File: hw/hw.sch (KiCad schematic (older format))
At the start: 36 parts, among them U1 74LS32, U10 74LS74, U2 Z80CPU, U3 74LS138, U4 74LS08, U5 CY7C199, U6 74LS299, U7 74HCT574, U8 74LS161, U9 74LS245, X1 CXO_DIP8

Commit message: move over to dedicated AVR
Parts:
- removed A1: Arduino_Nano_v3.x, Module:Arduino_Nano, symbol MCU_Module:Arduino_Nano_v3.x
- removed D1: 1N4148, Diode_THT:D_DO-35_SOD27_P7.62mm_Horizontal, symbol Diode:1N4148
- added C? (x2): 10n, symbol Device:C_Small
- added J?: Conn_02x03_Odd_Even, symbol Connector_Generic:Conn_02x03_Odd_Even
- added R?: 4K7, symbol Device:R
- added U?: ATmega328P-PU, Package_DIP:DIP-28_W7.62mm, symbol MCU_Microchip_ATmega:ATmega328P-PU
- added U? (x2): 74LS74, symbol 74xx:74LS74
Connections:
- net labels added: CLK_AVR, ISP_MISO, ISP_MOSI, ISP_RESET, ISP_SCLK, VIS, VIS_RAW
- wire segments 343 -> 383
- no-connect marks 30 -> 19
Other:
- note added: "ARDUINO at 0x80\nPORTA at 0x81"
- note added: "Close to pins 20 and 7"
- note added: "FIXME: delete this\n"

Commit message: got video display working well
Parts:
- removed U? (x2): 74LS74, symbol 74xx:74LS74
- added U?: 74LS74, symbol 74xx:74LS74
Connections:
- net VIS_RAW is gone; now on net VIS: U?.5 (PD3)
- net +5V: now also U?.1 (~R), U?.4 (~S)
- net CHAR_TC: now also U?.3 (C)
- net HSYNC: now also U?.5 (Q)
- net HSYNC_RAW: now also U?.2 (D)
- no-connect marks 19 -> 18
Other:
- note removed: "FIXME: delete this\n"
- note removed: "FIXME: sync vsync to hsync?"
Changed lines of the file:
@@
 Text GLabel 7000 5700 0    50   Input ~ 0
 ~DPY_PL
-Text Notes 12100 1600 0    50   ~ 0
-FIXME: sync vsync to hsync?
 $Comp
 L Connector:DB15_Female_HighDensity_MountingHoles J?
@@
 Wire Wire Line
 	-700 10100 -800 10100
-Text Notes 13800 1700 0    50   ~ 0
-FIXME: delete this\n
 Text GLabel -700 8100 2    50   Output ~ 0
 VSYNC
@@
 	-700 8100 -800 8100
 Text GLabel -700 9900 2    50   Output ~ 0
-VIS_RAW
+VIS
 Wire Wire Line
 	-700 9900 -800 9900
@@
 $Comp
 L 74xx:74LS74 U?
-U 2 1 5E1749F3
-P 17400 3200
-F 0 "U?" H 17250 3450 50  0000 C CNN
-F 1 "74LS74" H 17550 3450 50  0000 C CNN
-F 2 "" H 17400 3200 50  0001 C CNN
-F 3 "74xx/74hc_hct74.pdf" H 17400 3200 50  0001 C CNN
-	2    17400 3200
-	1    0    0    -1
-$EndComp
-$Comp
-L 74xx:74LS74 U?
-U 1 1 5E174A95
-P 17400 4300
-F 0 "U?" H 17250 4550 50  0000 C CNN
-F 1 "74LS74" H 17550 4550 50  0000 C CNN
-F 2 "" H 17400 4300 50  0001 C CNN
-F 3 "74xx/74hc_hct74.pdf" H 17400 4300 50  0001 C CNN
-	1    17400 4300
-	1    0    0    -1
-$EndComp
-Text GLabel 16900 4200 0    50   Input ~ 0
+U 1 1 5E5262C9
+P 15000 1300
+F 0 "U?" H 14850 1550 50  0000 C CNN
+F 1 "74LS74" H 15150 1550 50  0000 C CNN
+F 2 "" H 15000 1300 50  0001 C CNN
+F 3 "74xx/74hc_hct74.pdf" H 15000 1300 50  0001 C CNN
+	1    15000 1300
+	1    0    0    -1
+$EndComp
+Wire Wire Line
+	15000 900  15000 1000
+Wire Wire Line
+	14700 1200 14600 1200
+Wire Wire Line
+	14600 1700 15000 1700
+Wire Wire Line
+	15300 1200 15500 1200
+Text GLabel 15500 1200 2    50   Output ~ 0
+HSYNC
+Wire Wire Line
+	14600 1300 14700 1300
+Wire Wire Line
+	15000 1700 15000 1600
+$Comp
+L power:+5V #PWR?
+U 1 1 5E5262D6
+P 15000 900
+F 0 "#PWR?" H 15000 750 50  0001 C CNN
+F 1 "+5V" H 15015 1073 50  0000 C CNN
+F 2 "" H 15000 900 50  0001 C CNN
+F 3 "" H 15000 900 50  0001 C CNN
+	1    15000 900
+	1    0    0    -1
+$EndComp
+Text GLabel 14600 1200 0    50   Input ~ 0
 HSYNC_RAW
-Text GLabel 16900 3100 0    50   Input ~ 0
-VIS_RAW
-Wire Wire Line
-	16900 4200 17100 4200
-Wire Wire Line
-	16900 3100 17100 3100
-$Comp
-L power:+5V #PWR?
-U 1 1 5E28AFBB
-P 17400 2800
-F 0 "#PWR?" H 17400 2650 50  0001 C CNN
-F 1 "+5V" H 17415 2973 50  0000 C CNN
-F 2 "" H 17400 2800 50  0001 C CNN
-F 3 "" H 17400 2800 50  0001 C CNN
-	1    17400 2800
-	1    0    0    -1
-$EndComp
-Wire Wire Line
-	17400 2800 17400 2900
-$Comp
-L power:+5V #PWR?
-U 1 1 5E2B9A1E
-P 17400 3900
-F 0 "#PWR?" H 17400 3750 50  0001 C CNN
-F 1 "+5V" H 17415 4073 50  0000 C CNN
-F 2 "" H 17400 3900 50  0001 C CNN
-F 3 "" H 17400 3900 50  0001 C CNN
-	1    17400 3900
-	1    0    0    -1
-$EndComp
-Wire Wire Line
-	17400 3900 17400 4000
-$Comp
-L power:+5V #PWR?
-U 1 1 5E345A93
-P 17800 3500
-F 0 "#PWR?" H 17800 3350 50  0001 C CNN
-F 1 "+5V" H 17815 3673 50  0000 C CNN
-F 2 "" H 17800 3500 50  0001 C CNN
-F 3 "" H 17800 3500 50  0001 C CNN
-	1    17800 3500
-	1    0    0    -1
-$EndComp
-Wire Wire Line
-	17800 3500 17800 3550
-Wire Wire Line
-	17800 3550 17400 3550
-Wire Wire Line
-	17400 3550 17400 3500
-$Comp
-L power:+5V #PWR?
-U 1 1 5E374AC3
-P 17800 4600
-F 0 "#PWR?" H 17800 4450 50  0001 C CNN
-F 1 "+5V" H 17815 4773 50  0000 C CNN
-F 2 "" H 17800 4600 50  0001 C CNN
-F 3 "" H 17800 4600 50  0001 C CNN
-	1    17800 4600
-	1    0    0    -1
-$EndComp
-Wire Wire Line
-	17800 4600 17800 4650
-Wire Wire Line
-	17800 4650 17400 4650
-Wire Wire Line
-	17400 4650 17400 4600
-NoConn ~ 17700 4400
-NoConn ~ 17700 3300
-Text GLabel 17800 4200 2    50   Output ~ 0
-HSYNC
-Wire Wire Line
-	17800 4200 17700 4200
-Text GLabel 17800 3100 2    50   Output ~ 0
-VIS
-Wire Wire Line
-	17800 3100 17700 3100
-Text GLabel 16900 3300 0    50   Input ~ 0
+Text GLabel 14600 1300 0    50   Input ~ 0
 CHAR_TC
-Wire Wire Line
-	17100 3200 17000 3200
-Wire Wire Line
-	17000 3200 17000 3300
-Wire Wire Line
-	17000 3300 16900 3300
-Text GLabel 16900 4400 0    50   Input ~ 0
-CHAR_TC
-Wire Wire Line
-	17100 4300 17000 4300
-Wire Wire Line
-	17000 4300 17000 4400
-Wire Wire Line
-	17000 4400 16900 4400
+$Comp
+L power:+5V #PWR?
+U 1 1 5E5B3D83
+P 14600 1700
+F 0 "#PWR?" H 14600 1550 50  0001 C CNN
+F 1 "+5V" H 14615 1873 50  0000 C CNN
+F 2 "" H 14600 1700 50  0001 C CNN
+F 3 "" H 14600 1700 50  0001 C CNN
+	1    14600 1700
+	1    0    0    -1
+$EndComp
+NoConn ~ 15300 1400
 $EndSCHEMATC

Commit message: got stable screen display and demo program
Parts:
- added RN?: R_Network08_US, Resistor_THT:R_Array_SIP9, symbol Device:R_Network08_US
- added U?: 74LS32, symbol 74xx:74LS32
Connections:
- net D0: now also RN?.9 (R8)
- net D1: now also RN?.8 (R7)
- net D2: now also RN?.7 (R6)
- net D3: now also RN?.6 (R5)
- net D4: now also RN?.5 (R4)
- net D5: now also RN?.4 (R3)
- net D6: now also RN?.3 (R2)
- net D7: now also RN?.2 (R1)
- net GND: now also RN?.1 (common)
- net ~MEM_REQ: now also U?.4
- net ~REFRESH: now also U?.5; no longer U?.11 (Cp)
- new net ~RFSH_VALID: U?.11 (Cp), U?.6
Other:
- note added: "Open Question: sync VIS to CHAR_TC?"
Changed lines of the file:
@@
 	5600 5500 5500 5500
 Text GLabel 5500 5650 0    50   Input ~ 0
-~REFRESH
+~RFSH_VALID
 Wire Wire Line
 	5500 5650 5550 5650
@@
 $EndComp
 NoConn ~ 15300 1400
+Wire Wire Line
+	15100 6600 14900 6600
+Wire Wire Line
+	14900 6700 15100 6700
+Wire Wire Line
+	14900 6800 15100 6800
+Wire Wire Line
+	15100 6900 14900 6900
+Wire Wire Line
+	14900 7000 15100 7000
+Wire Wire Line
+	15100 7100 14900 7100
+Wire Wire Line
+	14900 7200 15100 7200
+Wire Wire Line
+	15100 7300 14900 7300
+$Comp
+L Device:R_Network08_US RN?
+U 1 1 5E64502A
+P 15300 6900
+F 0 "RN?" V 15817 6900 50  0000 C CNN
+F 1 "R_Network08_US" V 15726 6900 50  0000 C CNN
+F 2 "Resistor_THT:R_Array_SIP9" V 15775 6900 50  0001 C CNN
+F 3 "http://www.vishay.com/docs/31509/csc.pdf" H 15300 6900 50  0001 C CNN
+	1    15300 6900
+	0    1    -1   0
+$EndComp
+$Comp
+L power:GND #PWR?
+U 1 1 5E645031
+P 15600 7400
+F 0 "#PWR?" H 15600 7150 50  0001 C CNN
+F 1 "GND" H 15605 7227 50  0000 C CNN
+F 2 "" H 15600 7400 50  0001 C CNN
+F 3 "" H 15600 7400 50  0001 C CNN
+	1    15600 7400
+	1    0    0    -1
+$EndComp
+Wire Wire Line
+	15500 7300 15600 7300
+Wire Wire Line
+	15600 7300 15600 7400
+Text GLabel 14900 6600 0    50   BiDi ~ 0
+D0
+Text GLabel 14900 6700 0    50   BiDi ~ 0
+D1
+Text GLabel 14900 6800 0    50   BiDi ~ 0
+D2
+Text GLabel 14900 6900 0    50   BiDi ~ 0
+D3
+Text GLabel 14900 7000 0    50   BiDi ~ 0
+D4
+Text GLabel 14900 7100 0    50   BiDi ~ 0
+D5
+Text GLabel 14900 7200 0    50   BiDi ~ 0
+D6
+Text GLabel 14900 7300 0    50   BiDi ~ 0
+D7
+Text GLabel 1400 8800 0    50   Input ~ 0
+~MEM_REQ
+Text GLabel 1400 9000 0    50   Input ~ 0
+~REFRESH
+$Comp
+L 74xx:74LS32 U?
+U 2 1 5E76DC2D
+P 1900 8900
+F 0 "U?" H 1900 9225 50  0000 C CNN
+F 1 "74LS32" H 1900 9134 50  0000 C CNN
+F 2 "" H 1900 8900 50  0001 C CNN
+F 3 "http://www.ti.com/lit/gpn/sn74LS32" H 1900 8900 50  0001 C CNN
+	2    1900 8900
+	1    0    0    -1
+$EndComp
+Wire Wire Line
+	1400 9000 1600 9000
+Wire Wire Line
+	1600 8800 1400 8800
+Text GLabel 2400 8900 2    50   Output ~ 0
+~RFSH_VALID
+Wire Wire Line
+	2400 8900 2200 8900
+Text Notes 15400 1750 0    50   ~ 0
+Open Question: sync VIS to CHAR_TC?
 $EndSCHEMATC

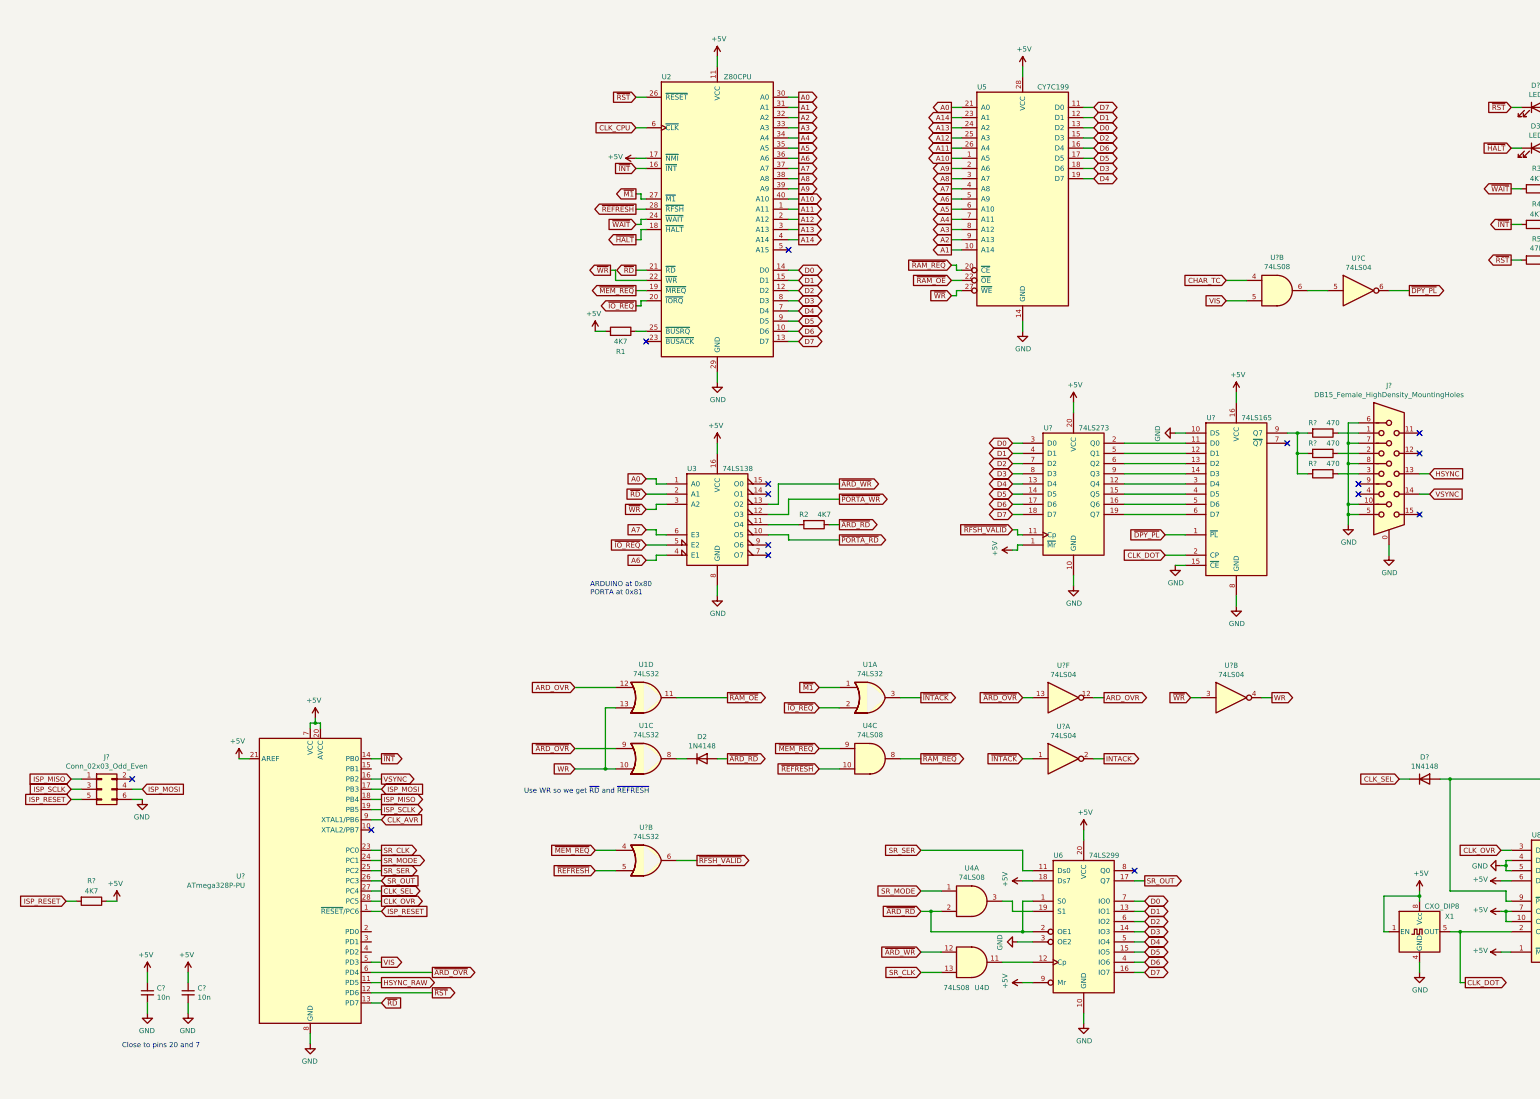
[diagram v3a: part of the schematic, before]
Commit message: fix schematic to match reality
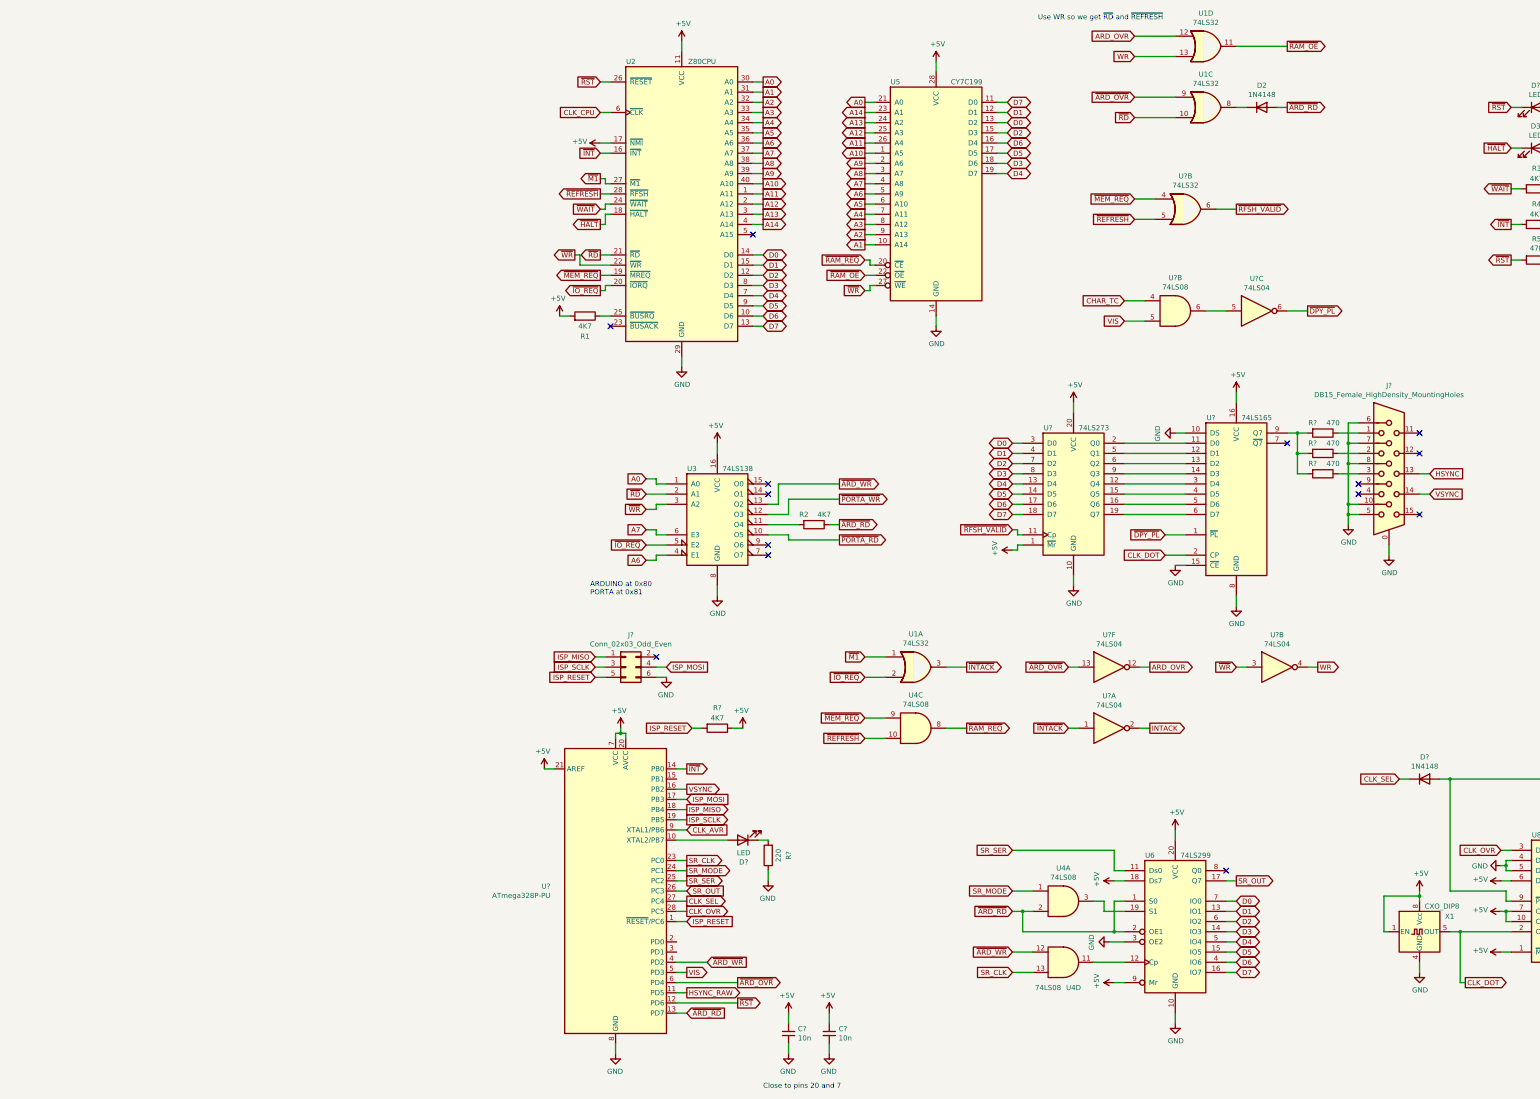
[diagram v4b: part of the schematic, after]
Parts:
- added D?: LED, symbol Device:LED
- added R?: 220, symbol Device:R
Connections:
- net GND: now also R?.1
- net WR: no longer U1.10
- net ~ARD_RD: now also U?.13 (PD7)
- net ~ARD_WR: now also U?.4 (PD2)
- net ~RD: now also U1.10; no longer U?.13 (PD7)
- net at U?.10 (XTAL2/PB7): now also D?.2 (A)
- new net: D?.1 (K), R?.2
- no-connect marks 18 -> 17
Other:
- moved on the sheet: C?, D2, J?, R1, R?, U1A, U1C, U1D, U2, U4A, U4C, U4D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
